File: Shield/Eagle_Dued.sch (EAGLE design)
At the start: 110 parts, among them IC1 7805TV, IC2 LM340MP-05

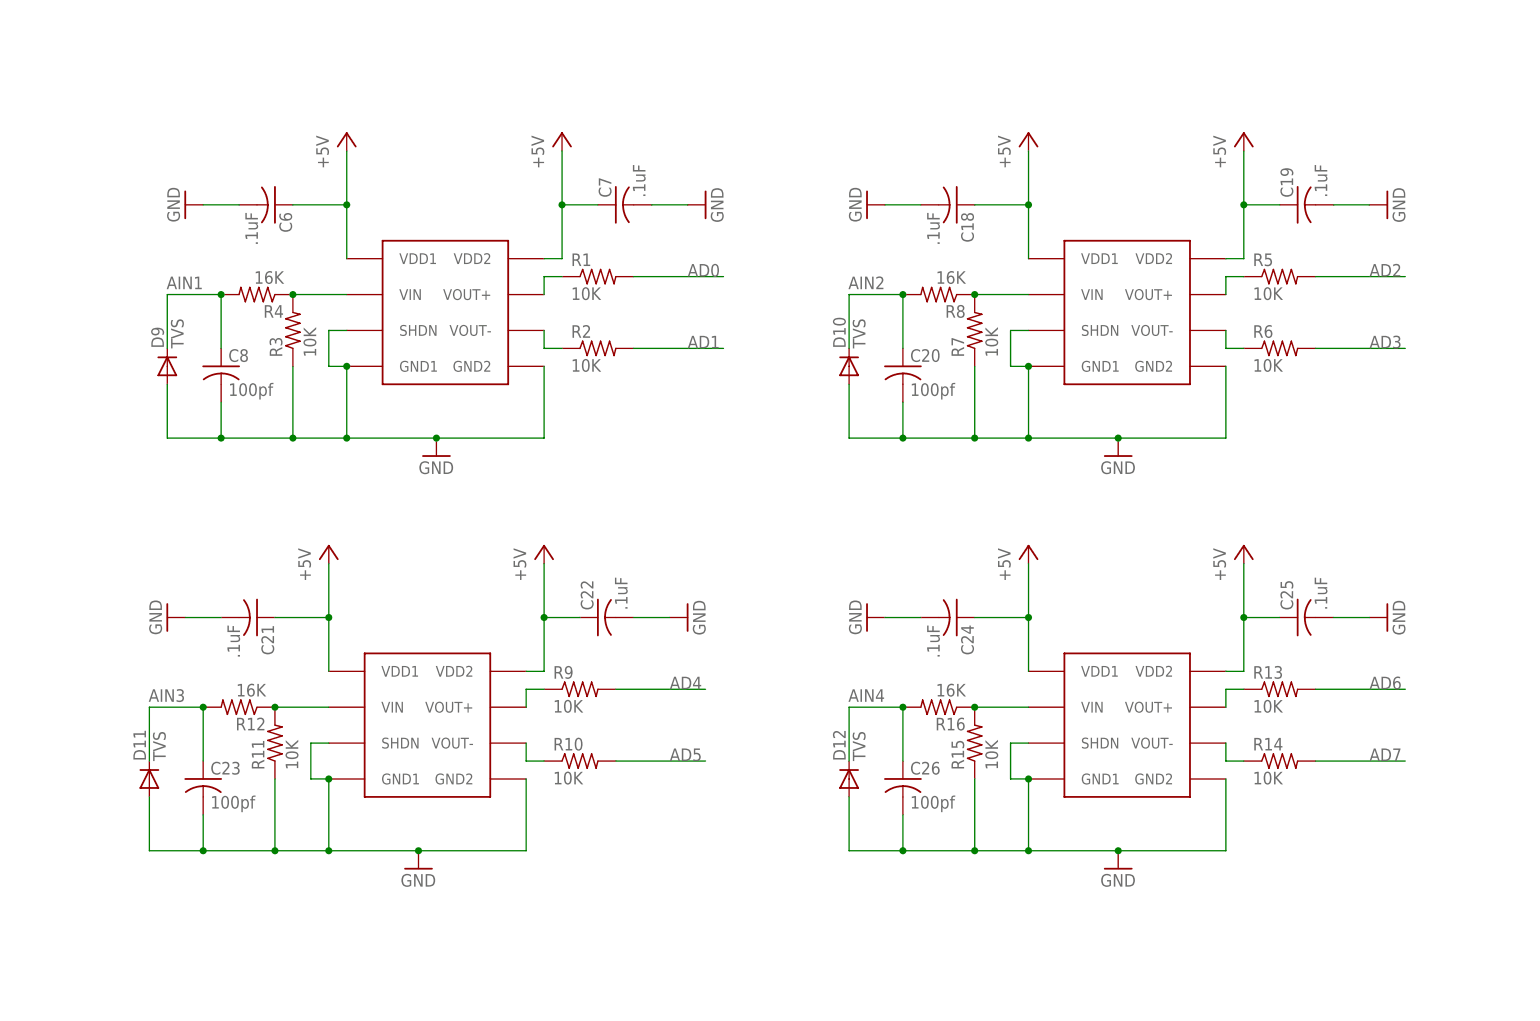
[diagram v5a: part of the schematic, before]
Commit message: Added analog shield, flipped Due on Dued board, fixed miniwifi footprint
Added an analog shield that will be used for all analog input instead of placing it on the main DueD board. Also, now all boards will be two layer instead of four.

Flipped over the Due on the DueD board. Now the DueD board is to have pins that stick up for the Due to
mate to.

Drastically improved the accuracy of the miniwifi layout.
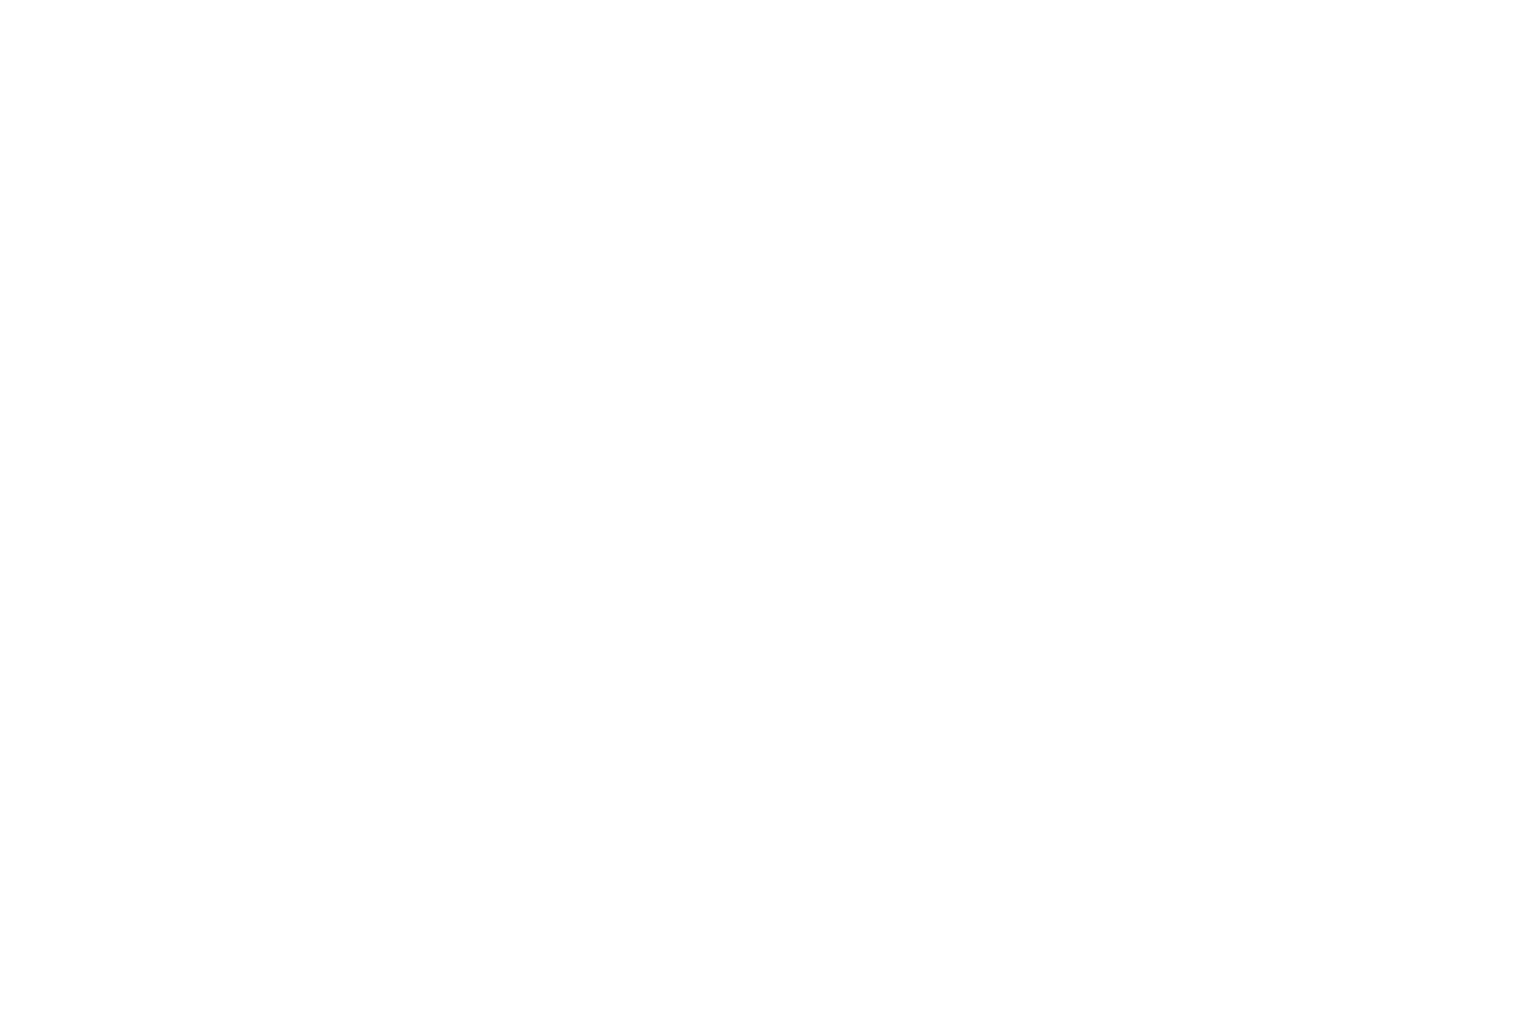
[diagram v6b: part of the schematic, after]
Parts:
- removed C18, C19, C21, C22, C24, C25, C6, C7: .1uF, rcl:C-USC0603
- removed C20, C23, C26, C8: 100pf, rcl:C-USC0603
- removed D10, D11, D12, D9: TVS, SparkFun-DiscreteSemi:DIODESOD
- removed R1, R10, R11, R13, R14, R15, R2, R3, R5, R6, R7, R9: 10K, rcl:R-US_R0603
- removed R12, R16, R4, R8: 16K, rcl:R-US_R0603
- removed U$1, U$10, U$11, U$12: ACPL-C87A-000E, ck_custom:ACPL-C87A-000E
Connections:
- removed net N$10: R3.2, R4.1, U$1.VIN
- removed net N$11: R7.2, R8.1, U$10.VIN
- removed net N$12: R5.1, U$10.VOUT+
- removed net N$13: R6.1, U$10.VOUT-
- removed net N$15: R11.2, R12.1, U$11.VIN
- removed net N$16: R9.1, U$11.VOUT+
- removed net N$17: R10.1, U$11.VOUT-
- removed net N$19: R15.2, R16.1, U$12.VIN
- removed net N$20: R13.1, U$12.VOUT+
- removed net N$21: R14.1, U$12.VOUT-
- removed net N$5: R1.1, U$1.VOUT+
- removed net N$7: R2.1, U$1.VOUT-
- net +5V: no longer C18.1, C19.1, C21.1, C22.1, C24.1, C25.1, C6.1, C7.1, U$1.VDD1, U$1.VDD2, U$10.VDD1, U$10.VDD2, U$11.VDD1, U$11.VDD2, U$12.VDD1, U$12.VDD2
- net AD0: no longer R1.2
- net AD1: no longer R2.2
- net AD2: no longer R5.2
- net AD3: no longer R6.2
- net AD4: no longer R9.2
- net AD5: no longer R10.2
- net AD6: no longer R13.2
- net AD7: no longer R14.2
- net AIN1: no longer C8.1, D9.C, R4.2
- net AIN2: no longer C20.1, D10.C, R8.2
- net AIN3: no longer C23.1, D11.C, R12.2
- net AIN4: no longer C26.1, D12.C, R16.2
- net GND: no longer C18.2, C19.2, C20.2, C21.2, C22.2, C23.2, C24.2, C25.2, C26.2, C6.2, C7.2, C8.2, D10.A, D11.A, D12.A, D9.A, R11.1, R15.1, R3.1, R7.1, U$1.GND1, U$1.GND2, U$1.SHDN, U$10.GND1, U$10.GND2, U$10.SHDN, U$11.GND1, U$11.GND2, U$11.SHDN, U$12.GND1, U$12.GND2, U$12.SHDN
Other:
- note removed: "ANALOG INPUTS"

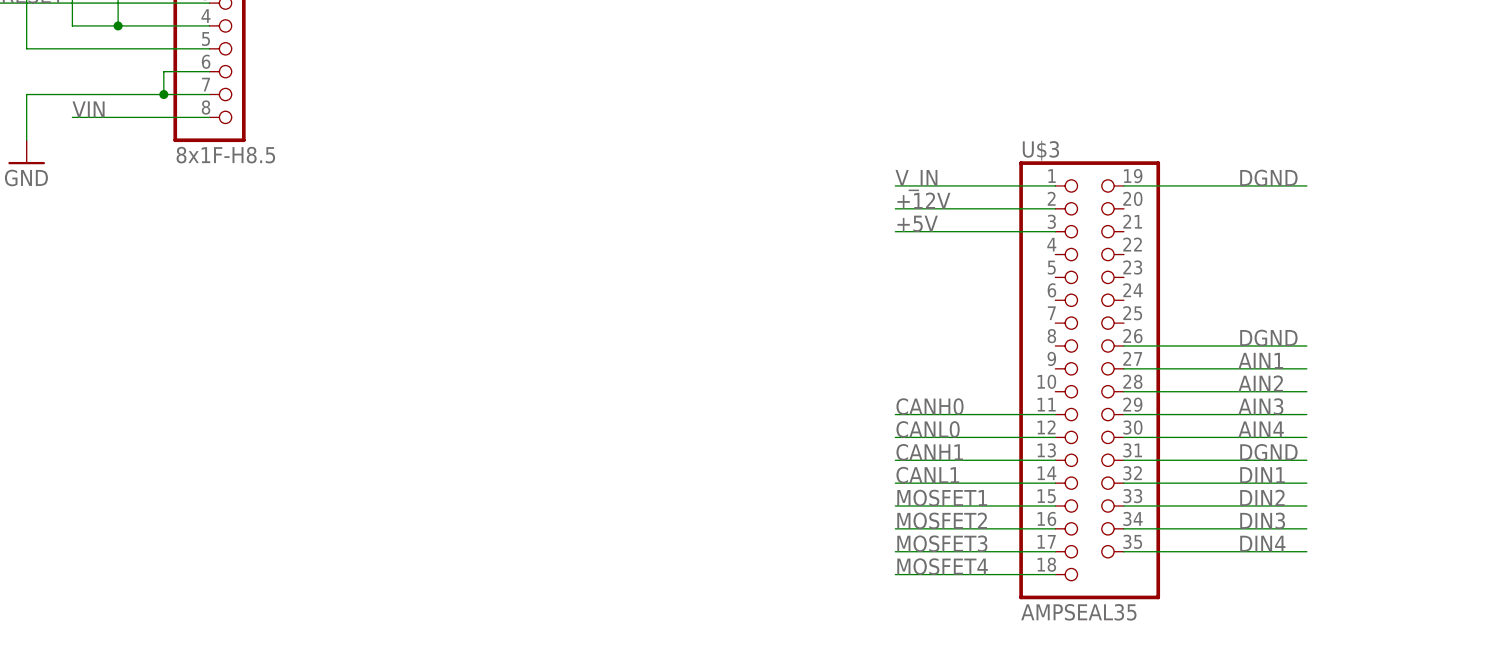
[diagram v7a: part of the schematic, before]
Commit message: Updated canbus board to be more correct, fixed size of ampseal connector, totally new DueD board.
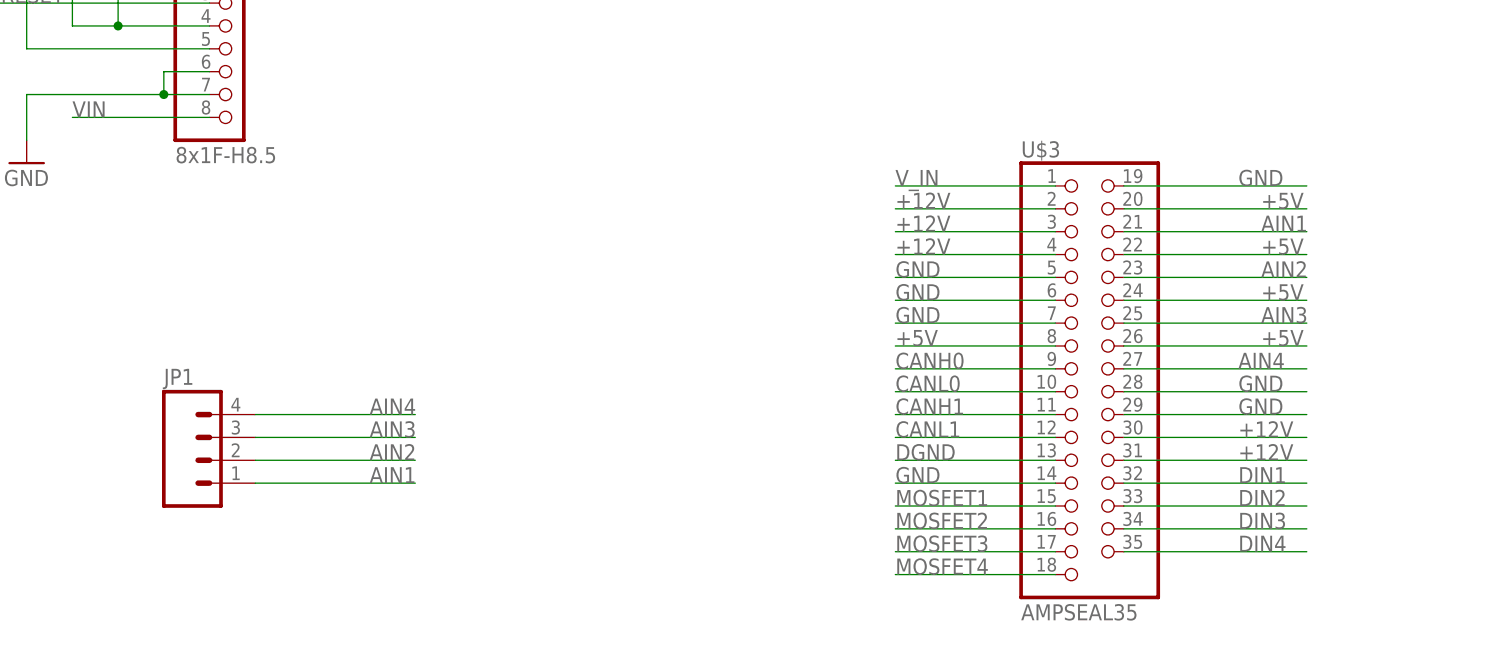
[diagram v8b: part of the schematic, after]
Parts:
- added JP1: (no value), SparkFun-Connectors:M04POLAR
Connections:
- net +12V: now also U$3.3, U$3.30, U$3.31, U$3.4
- net +5V: now also U$3.20, U$3.22, U$3.24, U$3.26, U$3.8; no longer U$3.3
- net AIN1: now also JP1.1, U$3.21; no longer U$3.27
- net AIN2: now also JP1.2, U$3.23; no longer U$3.28
- net AIN3: now also JP1.3, U$3.25; no longer U$3.29
- net AIN4: now also JP1.4, U$3.27; no longer U$3.30
- net CANH0: now also U$3.9; no longer U$3.11
- net CANH1: now also U$3.11; no longer U$3.13
- net CANL0: now also U$3.10; no longer U$3.12
- net CANL1: now also U$3.12; no longer U$3.14
- net DGND: now also U$3.13; no longer U$3.19, U$3.26, U$3.31
- net GND: now also U$3.14, U$3.19, U$3.28, U$3.29, U$3.5, U$3.6, U$3.7
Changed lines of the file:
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@@
 <part name="D13" library="SparkFun-LED" deviceset="LED-GREEN" device="0603" value="GREEN"/>
 <part name="GND25" library="supply1" deviceset="GND" device=""/>
+<part name="JP1" library="SparkFun-Connectors" deviceset="M04" device="POLAR"/>
 </parts>
 <sheets>
@@
 <instance part="D13" gate="G$1" x="495.3" y="88.9" rot="R90"/>
 <instance part="GND25" gate="1" x="510.54" y="88.9" rot="R90"/>
+<instance part="JP1" gate="G$1" x="449.58" y="137.16"/>
 </instances>
 <busses>
@@
 </segment>
 <segment>
-<pinref part="U$3" gate="G$1" pin="3"/>
-<wire x1="543.56" y1="162.56" x2="525.78" y2="162.56" width="0.1524" layer="91"/>
-<label x="525.78" y="162.56" size="1.778" layer="95"/>
+<pinref part="U$3" gate="G$1" pin="20"/>
+<wire x1="551.18" y1="165.1" x2="571.5" y2="165.1" width="0.1524" layer="91"/>
+<label x="566.42" y="165.1" size="1.778" layer="95"/>
+</segment>
+<segment>
+<pinref part="U$3" gate="G$1" pin="22"/>
+<wire x1="551.18" y1="160.02" x2="571.5" y2="160.02" width="0.1524" layer="91"/>
+<label x="566.42" y="160.02" size="1.778" layer="95"/>
+</segment>
+<segment>
+<pinref part="U$3" gate="G$1" pin="24"/>
+<wire x1="551.18" y1="154.94" x2="571.5" y2="154.94" width="0.1524" layer="91"/>
+<label x="566.42" y="154.94" size="1.778" layer="95"/>
+</segment>
+<segment>
+<pinref part="U$3" gate="G$1" pin="26"/>
+<wire x1="551.18" y1="149.86" x2="571.5" y2="149.86" width="0.1524" layer="91"/>
+<label x="566.42" y="149.86" size="1.778" layer="95"/>
+</segment>
+<segment>
+<pinref part="U$3" gate="G$1" pin="8"/>
+<wire x1="543.56" y1="149.86" x2="525.78" y2="149.86" width="0.1524" layer="91"/>
+<label x="525.78" y="149.86" size="1.778" layer="95"/>
 </segment>
 </net>
@@
 <wire x1="500.38" y1="88.9" x2="508" y2="88.9" width="0.1524" layer="91"/>
 </segment>
+<segment>
+<pinref part="U$3" gate="G$1" pin="14"/>
+<wire x1="543.56" y1="134.62" x2="525.78" y2="134.62" width="0.1524" layer="91"/>
+<label x="525.78" y="134.62" size="1.778" layer="95"/>
+</segment>
+<segment>
+<pinref part="U$3" gate="G$1" pin="7"/>
+<wire x1="543.56" y1="152.4" x2="525.78" y2="152.4" width="0.1524" layer="91"/>
+<label x="525.78" y="152.4" size="1.778" layer="95"/>
+</segment>
+<segment>
+<pinref part="U$3" gate="G$1" pin="6"/>
+<wire x1="543.56" y1="154.94" x2="525.78" y2="154.94" width="0.1524" layer="91"/>
+<label x="525.78" y="154.94" size="1.778" layer="95"/>
+</segment>
+<segment>
+<pinref part="U$3" gate="G$1" pin="5"/>
+<wire x1="543.56" y1="157.48" x2="525.78" y2="157.48" width="0.1524" layer="91"/>
+<label x="525.78" y="157.48" size="1.778" layer="95"/>
+</segment>
+<segment>
+<pinref part="U$3" gate="G$1" pin="19"/>
+<wire x1="551.18" y1="167.64" x2="571.5" y2="167.64" width="0.1524" layer="91"/>
+<label x="563.88" y="167.64" size="1.778" layer="95"/>
+</segment>
+<segment>
+<wire x1="551.18" y1="144.78" x2="571.5" y2="144.78" width="0.1524" layer="91"/>
+<label x="563.88" y="144.78" size="1.778" layer="95"/>
+<pinref part="U$3" gate="G$1" pin="28"/>
+</segment>
+<segment>
+<wire x1="551.18" y1="142.24" x2="571.5" y2="142.24" width="0.1524" layer="91"/>
+<label x="563.88" y="142.24" size="1.778" layer="95"/>
+<pinref part="U$3" gate="G$1" pin="29"/>
+</segment>
 </net>
 <net name="VIN" class="0">
@@
 </segment>
 <segment>
-<pinref part="U$3" gate="G$1" pin="19"/>
-<wire x1="551.18" y1="167.64" x2="571.5" y2="167.64" width="0.1524" layer="91"/>
-<label x="563.88" y="167.64" size="1.778" layer="95"/>
-</segment>
-<segment>
-<pinref part="U$3" gate="G$1" pin="26"/>
-<wire x1="551.18" y1="149.86" x2="571.5" y2="149.86" width="0.1524" layer="91"/>
-<label x="563.88" y="149.86" size="1.778" layer="95"/>
-</segment>
-<segment>
-<pinref part="U$3" gate="G$1" pin="31"/>
-<wire x1="551.18" y1="137.16" x2="571.5" y2="137.16" width="0.1524" layer="91"/>
-<label x="563.88" y="137.16" size="1.778" layer="95"/>
+<pinref part="U$3" gate="G$1" pin="13"/>
+<wire x1="543.56" y1="137.16" x2="525.78" y2="137.16" width="0.1524" layer="91"/>
+<label x="525.78" y="137.16" size="1.778" layer="95"/>
 </segment>
 </net>
@@
 <label x="525.78" y="165.1" size="1.778" layer="95"/>
 </segment>
-</net>
-<net name="AIN4" class="0">
+<segment>
+<pinref part="U$3" gate="G$1" pin="31"/>
+<wire x1="551.18" y1="137.16" x2="571.5" y2="137.16" width="0.1524" layer="91"/>
+<label x="563.88" y="137.16" size="1.778" layer="95"/>
+</segment>
 <segment>
 <wire x1="551.18" y1="139.7" x2="571.5" y2="139.7" width="0.1524" layer="91"/>
@@
 <pinref part="U$3" gate="G$1" pin="30"/>
 </segment>
+<segment>
+<pinref part="U$3" gate="G$1" pin="3"/>
+<wire x1="543.56" y1="162.56" x2="525.78" y2="162.56" width="0.1524" layer="91"/>
+<label x="525.78" y="162.56" size="1.778" layer="95"/>
+</segment>
+<segment>
+<pinref part="U$3" gate="G$1" pin="4"/>
+<wire x1="543.56" y1="160.02" x2="525.78" y2="160.02" width="0.1524" layer="91"/>
+<label x="525.78" y="160.02" size="1.778" layer="95"/>
+</segment>
 </net>
 <net name="AIN3" class="0">
 <segment>
-<wire x1="551.18" y1="142.24" x2="571.5" y2="142.24" width="0.1524" layer="91"/>
-<label x="563.88" y="142.24" size="1.778" layer="95"/>
-<pinref part="U$3" gate="G$1" pin="29"/>
+<pinref part="U$3" gate="G$1" pin="25"/>
+<wire x1="551.18" y1="152.4" x2="571.5" y2="152.4" width="0.1524" layer="91"/>
+<label x="566.42" y="152.4" size="1.778" layer="95"/>
+</segment>
+<segment>
+<pinref part="JP1" gate="G$1" pin="3"/>
+<wire x1="454.66" y1="139.7" x2="472.44" y2="139.7" width="0.1524" layer="91"/>
+<label x="467.36" y="139.7" size="1.778" layer="95"/>
 </segment>
 </net>
 <net name="AIN2" class="0">
 <segment>
-<wire x1="551.18" y1="144.78" x2="571.5" y2="144.78" width="0.1524" layer="91"/>
-<label x="563.88" y="144.78" size="1.778" layer="95"/>
-<pinref part="U$3" gate="G$1" pin="28"/>
+<pinref part="U$3" gate="G$1" pin="23"/>
+<wire x1="551.18" y1="157.48" x2="571.5" y2="157.48" width="0.1524" layer="91"/>
+<label x="566.42" y="157.48" size="1.778" layer="95"/>
+</segment>
+<segment>
+<pinref part="JP1" gate="G$1" pin="2"/>
+<wire x1="454.66" y1="137.16" x2="472.44" y2="137.16" width="0.1524" layer="91"/>
+<label x="467.36" y="137.16" size="1.778" layer="95"/>
 </segment>
 </net>
 <net name="AIN1" class="0">
 <segment>
-<wire x1="551.18" y1="147.32" x2="571.5" y2="147.32" width="0.1524" layer="91"/>
-<label x="563.88" y="147.32" size="1.778" layer="95"/>
-<pinref part="U$3" gate="G$1" pin="27"/>
+<pinref part="U$3" gate="G$1" pin="21"/>
+<wire x1="551.18" y1="162.56" x2="571.5" y2="162.56" width="0.1524" layer="91"/>
+<label x="566.42" y="162.56" size="1.778" layer="95"/>
+</segment>
+<segment>
+<pinref part="JP1" gate="G$1" pin="1"/>
+<wire x1="454.66" y1="134.62" x2="472.44" y2="134.62" width="0.1524" layer="91"/>
+<label x="467.36" y="134.62" size="1.778" layer="95"/>
 </segment>
 </net>
@@
 <net name="CANL1" class="0">
 <segment>
-<wire x1="525.78" y1="134.62" x2="543.56" y2="134.62" width="0.1524" layer="91"/>
-<label x="525.78" y="134.62" size="1.778" layer="95"/>
-<pinref part="U$3" gate="G$1" pin="14"/>
-</segment>
-<segment>
 <pinref part="U$2" gate="G$1" pin="CANL"/>
 <wire x1="637.54" y1="-187.96" x2="652.78" y2="-187.96" width="0.1524" layer="91"/>
@@
 <pinref part="SJ4" gate="1" pin="1"/>
 </segment>
+<segment>
+<wire x1="525.78" y1="139.7" x2="543.56" y2="139.7" width="0.1524" layer="91"/>
+<label x="525.78" y="139.7" size="1.778" layer="95"/>
+<pinref part="U$3" gate="G$1" pin="12"/>
+</segment>
 </net>
 <net name="CANH1" class="0">
-<segment>
-<wire x1="525.78" y1="137.16" x2="543.56" y2="137.16" width="0.1524" layer="91"/>
-<label x="525.78" y="137.16" size="1.778" layer="95"/>
-<pinref part="U$3" gate="G$1" pin="13"/>
-</segment>
 <segment>
 <pinref part="U$2" gate="G$1" pin="CANH"/>
@@
 <pinref part="SJ3" gate="1" pin="1"/>
 </segment>
-</net>
-<net name="CANH0" class="0">
 <segment>
 <wire x1="525.78" y1="142.24" x2="543.56" y2="142.24" width="0.1524" layer="91"/>
@@
 <pinref part="U$3" gate="G$1" pin="11"/>
 </segment>
+</net>
+<net name="CANH0" class="0">
 <segment>
 <pinref part="U$6" gate="G$1" pin="CANH"/>
@@
 <pinref part="SJ1" gate="1" pin="1"/>
 </segment>
+<segment>
+<pinref part="U$3" gate="G$1" pin="9"/>
+<wire x1="543.56" y1="147.32" x2="525.78" y2="147.32" width="0.1524" layer="91"/>
+<label x="525.78" y="147.32" size="1.778" layer="95"/>
+</segment>
 </net>
 <net name="CANL0" class="0">
-<segment>
-<wire x1="525.78" y1="139.7" x2="543.56" y2="139.7" width="0.1524" layer="91"/>
-<label x="525.78" y="139.7" size="1.778" layer="95"/>
-<pinref part="U$3" gate="G$1" pin="12"/>
-</segment>
 <segment>
 <pinref part="U$6" gate="G$1" pin="CANL"/>
@@
 <label x="640.08" y="-129.54" size="1.778" layer="95"/>
 <pinref part="SJ2" gate="1" pin="1"/>
+</segment>
+<segment>
+<pinref part="U$3" gate="G$1" pin="10"/>
+<wire x1="543.56" y1="144.78" x2="525.78" y2="144.78" width="0.1524" layer="91"/>
+<label x="525.78" y="144.78" size="1.778" layer="95"/>
 </segment>
 </net>
@@
 </segment>
 </net>
+<net name="AIN4" class="0">
+<segment>
+<wire x1="551.18" y1="147.32" x2="571.5" y2="147.32" width="0.1524" layer="91"/>
+<label x="563.88" y="147.32" size="1.778" layer="95"/>
+<pinref part="U$3" gate="G$1" pin="27"/>
+</segment>
+<segment>
+<pinref part="JP1" gate="G$1" pin="4"/>
+<wire x1="454.66" y1="142.24" x2="472.44" y2="142.24" width="0.1524" layer="91"/>
+<label x="467.36" y="142.24" size="1.778" layer="95"/>
+</segment>
+</net>
